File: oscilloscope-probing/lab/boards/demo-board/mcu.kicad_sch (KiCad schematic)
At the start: 3 parts, among them J4 CORTEX_DEBUG_ETM, U4 XC7A35T-2FGG484I, U5 STM32H750XBH6

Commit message: Finished initial demo board schematic
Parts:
- added C59, C60, C61, C67, C68, C69, C71, C72, C73, C74, C75, C76, C77, C78, C79, C80, C81, C82, C83, C84, C85, C86, C87, C88, C89, C99: 0.47 uF, azonenberg_pcb:EIA_0402_CAP_NOSILK, symbol device:C
- added C62, C63, C64, C65, C66, C70: 4.7 uF, azonenberg_pcb:EIA_0603_CAP_NOSILK, symbol device:C
- added D4, D5, D6, D7: GREEN, azonenberg_pcb:EIA_0402_LED, symbol device:LED
- added FB2: MI0603J601R-10, azonenberg_pcb:EIA_0603_INDUCTOR_NOSILK, symbol passive-azonenberg:FERRITE_SMALL2
- added J6: CONN_01X06, symbol conn:CONN_01X06
- added R26: 10K, azonenberg_pcb:EIA_0402_RES_NOSILK, symbol device:R
- added R27: 100K, azonenberg_pcb:EIA_0402_RES_NOSILK, symbol device:R
- added R28, R29, R47, R48, R49, R50: 33, azonenberg_pcb:EIA_0402_RES_NOSILK, symbol device:R
- added R30, R31, R32, R33, R35, R38: 33, symbol device:R
- added R34, R44, R45, R46: 4.7K, symbol device:R
- added R39, R41, R42, R43: 33K, azonenberg_pcb:EIA_0402_RES_NOSILK, symbol device:R
- added SW3, SW4, SW5, SW6, SW7: SWITCH, azonenberg_pcb:SWITCH_RAFI_MICON_5, symbol passive-azonenberg:SWITCH
- added TP12: TESTCLIP, symbol conn:CONN_01X01
- added TP8: CONN_01X03, azonenberg_pcb:CONN_HEADER_2.54MM_1x3_REFLOW, symbol conn:CONN_01X03
- added TP9: U.FL, symbol conn:CONN_COAXIAL
- added U6, U7: ECS-1612MV-250-CN, azonenberg_pcb:OSCILLATOR_1.6x1.2, symbol osc-azonenberg:OSC
- added U8: W25Q80BV, symbol memory-azonenberg:W25Q80BV
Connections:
- net 3V3: now also U5.A6 (VDDLDO), U5.B1 (VBAT), U5.C17 (VDDLDO), U5.E7 (PDR_ON), U5.F17 (VDD33USB), U5.U12 (VDDLDO), C60.1, C61.1, C63.1, C64.1, C65.1, C67.1, C68.1, C69.1, C71.1, C72.1, C73.1, C75.1, C76.1, C77.1, C78.1, C79.1, C80.1, C81.1, C82.1, C83.1, C84.1, C85.1, C86.1, C87.1, C88.1, C89.1, C99.1, FB2.1, R26.1, R44.1, R45.1, R46.1, SW3.1, SW4.1, SW5.1, SW6.1, SW7.1, U6.1 (E/D#), U6.4 (Vdd), U7.1 (E/D#), U7.4 (Vdd), U8.8 (VCC)
- net FPGA_CCLK: now also U8.6 (CLK)
- net GND: now also U5.N1 (VREF_N), C59.1, C60.2, C61.2, C62.2, C63.2, C64.2, C65.2, C66.2, C67.2, C68.2, C69.2, C70.2, C71.2, C72.2, C73.2, C74.2, C75.2, C76.2, C77.2, C78.2, C79.2, C80.2, C81.2, C82.2, C83.2, C84.2, C85.2, C86.2, C87.2, C88.2, C89.2, C99.2, D4.1 (K), D5.1 (K), D6.1 (K), D7.1 (K), J6.1 (P1), R27.1, R34.1, TP8.3 (P3), TP9.2 (Ext), U6.2 (Vss), U7.2 (Vss), U8.4 (GND)
- net JTAG_TCK: now also U5.B14 (PA14)
- net JTAG_TDI: now also U5.A14 (PA15)
- net JTAG_TDO: now also R38.1
- net JTAG_TMS: now also U5.C15 (PA13)
- net MCU_DONE: now also U5.G4 (PF0)
- net MCU_RST_N: now also C59.2, R26.2, R27.2
- net SUPER_I2C_SCL: now also U5.D5 (PB8)
- net SUPER_I2C_SDA: now also U5.D4 (PB9)
- net TRACECLK: now also U5.C3 (PE2)
- net TRACED0: now also U5.D9 (PG13)
- net TRACED1: now also U5.D8 (PG14)
- net TRACED2: now also U5.D12 (PD2)
- net TRACED3: now also U5.C12 (PC12)
- net UART_CTS_N: now also U5.U5 (PB0)
- net UART_RTS_N: now also U5.U15 (PB14)
- net UART_RX: now also U5.N4 (PA1)
- net UART_TX: now also U5.N5 (PA0)
- net MCU_TRIG: now reaches U5.A16 (PI0)
- net MCU_TRIG: now also TP12.1 (P1)
- net DPAD_SEL: now reaches U5.D10 (PJ14)
- net DPAD_SEL: now also SW7.2
- net DPAD_S: now reaches U5.D11 (PJ12)
- net DPAD_S: now also SW6.2
- net DPAD_N: now reaches U5.E10 (PJ13)
- net DPAD_N: now also SW5.2
- net DPAD_E: now reaches U5.K14 (PJ11)
- net DPAD_E: now also SW4.2
- net DPAD_W: now reaches U5.L14 (PJ10)
- net DPAD_W: now also SW3.2
- net MCU_LED0: now reaches U5.N6 (PJ0)
- net MCU_LED0: now also R39.1
- net MCU_LED1: now reaches U5.P6 (PJ1)
- net MCU_LED1: now also R41.1
- net MCU_LED2: now reaches U5.T6 (PJ2)
- net MCU_LED2: now also R42.1
- net MCU_LED3: now reaches U5.U6 (PJ3)
- net MCU_LED3: now also R43.1
- net VCORE: now reaches U5.A7 (VCAP)
- net VCORE: now also U5.D17 (VCAP), U5.U11 (VCAP), C62.1, C66.1, TP9.1 (In)
- net A3V3: now reaches U5.L1 (VDDA)
- net A3V3: now also U5.M1 (VREF_P), C70.1, C74.1, FB2.2
- net CONSOLE_UART_RX: now reaches U5.D14 (PA10)
- net CONSOLE_UART_RX: now also TP8.2 (P2)
- net CONSOLE_UART_TX: now reaches U5.D15 (PA9)
- net CONSOLE_UART_TX: now also TP8.1 (P1)
- net DAC1_OUT2: now reaches U5.T3 (PA5)
- net DAC1_OUT1: now reaches U5.U3 (PA4)
- net MCU_CLK_25MHZ: now reaches U5.J2 (PH0)
- net MCU_CLK_25MHZ: now also R28.1
- net DPY_BS: now reaches U5.H4 (PF3)
- net DPY_DC: now reaches U5.J4 (PF5)
- net DPY_BUSY_N: now reaches U5.J5 (PF4)
- net DPY_SPI_CS_N: now reaches U5.K2 (PF6)
- net DPY_SPI_SCK: now reaches U5.K3 (PF7)
- net DPY_RST_N: now reaches U5.K4 (PF8)
- net DPY_SPI_DATA: now reaches U5.L4 (PF9)
- net FMC_NE3: now reaches U4.AA18 (IO_L17P_T2_A14_D30_14)
- net FMC_NE3: now also U5.G15 (PG6)
- net FPGA_UART_RTS_N: now reaches U4.AA19 (IO_L15P_T2_DQS_RDWR_B_14)
- net FPGA_UART_RTS_N: now also J6.6 (P6)
- net FMC_NOE: now reaches U4.AA20 (IO_L8P_T1_D11_14)
- net FMC_NOE: now also U5.A12 (PD4)
- net FMC_NWE: now reaches U4.AA21 (IO_L8N_T1_D12_14)
- net FMC_NWE: now also U5.A11 (PD5)
- net FMC_AD0: now reaches U4.AB18 (IO_L17N_T2_A13_D29_14)
- net FMC_AD0: now also U5.P16 (PD14)
- net FMC_NE4: now reaches U4.AB20 (IO_L15N_T2_DQS_DOUT_CSO_B_14)
- net FMC_NE4: now also U5.C9 (PG12)
- net FMC_A16: now reaches U4.AB21 (IO_L10P_T1_D14_14)
- net FMC_A16: now also U5.R15 (PD11)
- net FMC_A17: now reaches U4.AB22 (IO_L10N_T1_D15_14)
- net FMC_A17: now also U5.R16 (PD12)
- net FMC_AD11: now reaches U4.N13 (IO_L23P_T3_A03_D19_14)
- net FMC_AD11: now also U5.U10 (PE14)
- net FMC_AD12: now reaches U4.N14 (IO_L23N_T3_A02_D18_14)
- net FMC_AD12: now also U5.R11 (PE15)
- net FMC_AD15: now reaches U4.N15 (IO_25_14)
- net FMC_AD15: now also U5.T16 (PD10)
- net FMC_AD7: now reaches U4.N17 (IO_L21P_T3_DQS_14)
- net FMC_AD7: now also U5.N9 (PE10)
- net FMC_AD3: now reaches U4.P14 (IO_L19P_T3_A10_D26_14)
- net FMC_AD3: now also U5.E12 (PD1)
- net FMC_AD9: now reaches U4.P15 (IO_L22P_T3_A05_D21_14)
- net FMC_AD9: now also U5.R10 (PE12)
- net FMC_AD13: now reaches U4.P16 (IO_L24P_T3_A01_D17_14)
- net FMC_AD13: now also U5.U16 (PD8)
- net FMC_AD8: now reaches U4.P17 (IO_L21N_T3_DQS_A06_D22_14)
- net FMC_AD8: now also U5.P10 (PE11)
- net FPGA_UART_TX: now reaches U4.P19 (IO_L5P_T0_D06_14)
- net FPGA_UART_TX: now also J6.4 (P4)
- net at U4.P21 (IO_L2P_T0_D02_14): now also R32.2
- net at U4.P22 (IO_L1P_T0_D00_MOSI_14): now also R30.2
- net FMC_AD4: now reaches U4.R14 (IO_L19N_T3_A09_D25_VREF_14)
- net FMC_AD4: now also U5.U9 (PE7)
- net FMC_AD10: now reaches U4.R16 (IO_L22N_T3_A04_D20_14)
- net FMC_AD10: now also U5.T10 (PE13)
- net FMC_AD14: now reaches U4.R17 (IO_L24N_T3_A00_D16_14)
- net FMC_AD14: now also U5.T17 (PD9)
- net FMC_AD5: now reaches U4.R18 (IO_L20P_T3_A08_D24_14)
- net FMC_AD5: now also U5.T9 (PE8)
- net FPGA_UART_RX: now reaches U4.R19 (IO_L5N_T0_D07_14)
- net FPGA_UART_RX: now also J6.5 (P5)
- net at U4.R21 (IO_L2N_T0_D03_14): now also R33.2
- net at U4.R22 (IO_L1N_T0_D01_DIN_14): now also R31.2
- net FMC_AD6: now reaches U4.T18 (IO_L20N_T3_A07_D23_14)
- net FMC_AD6: now also U5.P9 (PE9)
- net at U4.T19 (IO_L6P_T0_FCS_B_14): now also R35.2
- net FMC_A21: now reaches U4.T21 (IO_L4P_T0_D04_14)
- net FMC_A21: now also U5.D1 (PE5)
- net FMC_AD1: now reaches U4.U17 (IO_L18P_T2_A12_D28_14)
- net FMC_AD1: now also U5.P15 (PD15)
- net FMC_AD2: now reaches U4.U18 (IO_L18N_T2_A11_D27_14)
- net FMC_AD2: now also U5.D13 (PD0)
- net FMC_A18: now reaches U4.U20 (IO_L11P_T1_SRCC_14)
- net FMC_A18: now also U5.R17 (PD13)
- net FMC_A22: now reaches U4.U21 (IO_L4N_T0_D05_14)
- net FMC_A22: now also U5.E5 (PE6)
- net at U4.U22 (IO_L3P_T0_DQS_PUDC_B_14): now also R34.2
- net FMC_NE1: now reaches U4.V17 (IO_L16P_T2_CSI_B_14)
- net FMC_NE1: now also U5.C11 (PD7)
- net FPGA_UART_CTS_N: now reaches U4.V19 (IO_L14N_T2_SRCC_14)
- net FPGA_UART_CTS_N: now also J6.2 (P2)
- net FMC_A19: now reaches U4.V20 (IO_L11N_T1_SRCC_14)
- net FMC_A19: now also U5.D3 (PE3)
- net FMC_A20: now reaches U4.V22 (IO_L3N_T0_DQS_EMCCLK_14)
- net FMC_A20: now also U5.D2 (PE4)
- net FMC_NE2: now reaches U4.W17 (IO_L16N_T2_A15_D31_14)
- net FMC_NE2: now also U5.E13 (PC8)
- net FPGA_CLK_25MHZ: now reaches U4.W19 (IO_L12P_T1_MRCC_14)
- net FPGA_CLK_25MHZ: now also R29.1
- net FMC_NL_NADV: now reaches U4.W21 (IO_L7P_T1_D09_14)
- net FMC_NL_NADV: now also U5.C5 (PB7)
- net FMC_NWAIT: now reaches U4.W22 (IO_L7N_T1_D10_14)
- net FMC_NWAIT: now also U5.B11 (PD6)
- net FMC_CLK: now reaches U4.Y18 (IO_L13P_T2_MRCC_14)
- net FMC_CLK: now also U5.B12 (PD3)
- net FMC_NBL0: now reaches U4.Y21 (IO_L9P_T1_DQS_14)
- net FMC_NBL0: now also U5.C4 (PE0)
- net FMC_NBL1: now reaches U4.Y22 (IO_L9N_T1_DQS_D13_14)
- net FMC_NBL1: now also U5.B4 (PE1)
- net at U5.C6 (PB3): now also R38.2
- new net: D4.2 (A), R39.2
- new net: R48.2, U8.5 (DI/IO0)
- new net: R29.2, U7.3 (CLK)
- new net: D5.2 (A), R41.2
- new net: R28.2, U6.3 (CLK)
- new net: D6.2 (A), R42.2
- new net: R49.1, U8.2 (DO/IO1)
- new net: R50.1, U8.3 (WP#/IO2)
- new net: R47.2, U8.7 (HOLD#/IO3)
- new net: D7.2 (A), R43.2
- new net QSPI_CS_N: R35.1, R46.2, U8.1 (CS#)
- new net QSPI_DQ0: R30.1, R48.1
- new net QSPI_DQ1: R31.1, R49.2
- new net QSPI_DQ2: R32.1, R44.2, R50.2
- new net QSPI_DQ3: R33.1, R45.2, R47.1
- no-connect marks 8 -> 115
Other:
- added sheet E-paper display (display.kicad_sch)
- note added: "FTDI cable pinout"
- note added: "MCU VDDA decoupling"
- note added: "TRACECLK / A23 unavoidably conflict So limit to 2^22 words (2^23 = 0x80_0000 bytes) of APB address space"
- note added: "VCAP"
- note added: "VDD"
- note added: "VDD33USB"
- note added: "VDDLDO"

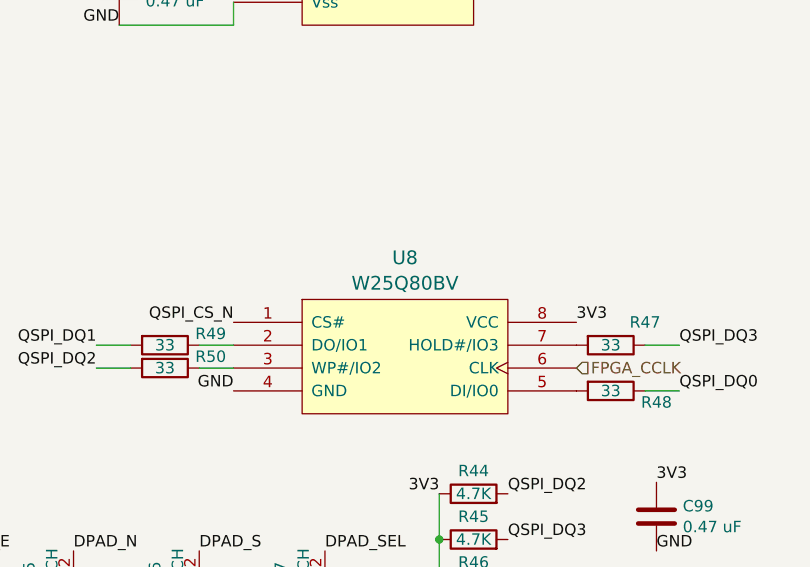
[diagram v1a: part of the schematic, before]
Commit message: Continued initial schematic, assigned footprints
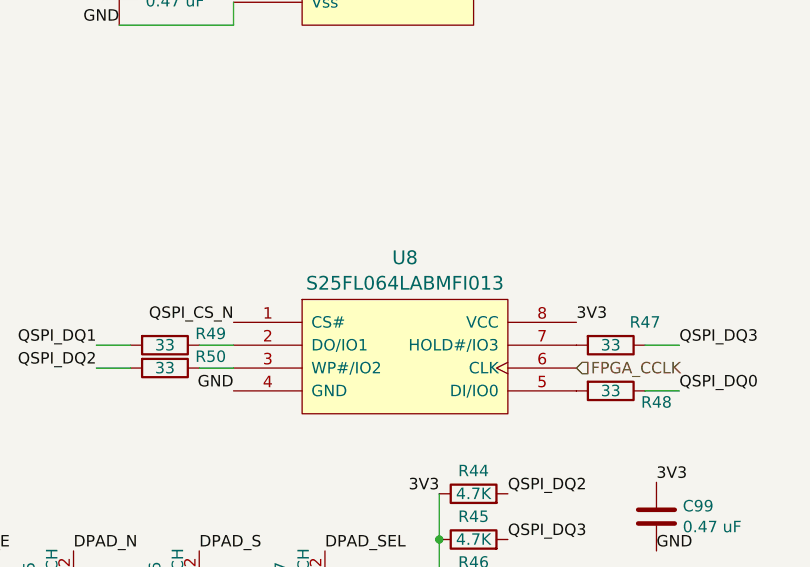
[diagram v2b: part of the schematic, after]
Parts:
- J6: footprint (none) -> azonenberg_pcb:CONN_HEADER_2.54MM_1x6_REFLOW
- R30, R31, R32, R33, R34, R35, R38, R44, R45, R46: footprint (none) -> azonenberg_pcb:EIA_0402_RES_NOSILK
- TP12: footprint (none) -> azonenberg_pcb:TESTPOINT_SMT_KEYSTONE_5016
- TP9: footprint (none) -> azonenberg_pcb:CONN_U.FL_TE_1909763-1
- U4: footprint (none) -> azonenberg_pcb:BGA_484_22x22_FULLARRAY_1MM
- U5: footprint (none) -> azonenberg_pcb:BGA_265_14x14_DEPOP_0.8MM
- U8: value W25Q80BV -> S25FL064LABMFI013; footprint (none) -> azonenberg_pcb:SOIC_8_5.3MM
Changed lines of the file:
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@@
 			)
 		)
-		(property "Footprint" ""
+		(property "Footprint" "azonenberg_pcb:BGA_265_14x14_DEPOP_0.8MM"
 			(at 111.76 209.55 0)
 			(effects
@@
 			)
 		)
-		(property "Footprint" ""
+		(property "Footprint" "azonenberg_pcb:BGA_265_14x14_DEPOP_0.8MM"
 			(at 111.76 256.54 0)
 			(effects
@@
 			)
 		)
-		(property "Footprint" ""
+		(property "Footprint" "azonenberg_pcb:EIA_0402_RES_NOSILK"
 			(at 31.75 80.518 90)
 			(effects
@@
 			)
 		)
-		(property "Footprint" ""
+		(property "Footprint" "azonenberg_pcb:BGA_265_14x14_DEPOP_0.8MM"
 			(at 254 78.74 0)
 			(effects
@@
 			)
 		)
-		(property "Footprint" ""
+		(property "Footprint" "azonenberg_pcb:EIA_0402_RES_NOSILK"
 			(at 185.42 274.828 90)
 			(effects
@@
 			)
 		)
-		(property "Footprint" ""
+		(property "Footprint" "azonenberg_pcb:EIA_0402_RES_NOSILK"
 			(at 341.63 33.528 90)
 			(effects
@@
 			)
 		)
-		(property "Footprint" ""
+		(property "Footprint" "azonenberg_pcb:BGA_265_14x14_DEPOP_0.8MM"
 			(at 162.56 43.18 0)
 			(effects
@@
 			)
 		)
-		(property "Footprint" ""
+		(property "Footprint" "azonenberg_pcb:BGA_265_14x14_DEPOP_0.8MM"
 			(at 39.37 63.5 0)
 			(effects
@@
 			)
 		)
-		(property "Footprint" ""
+		(property "Footprint" "azonenberg_pcb:EIA_0402_RES_NOSILK"
 			(at 185.42 264.668 90)
 			(effects
@@
 			)
 		)
-		(property "Footprint" ""
+		(property "Footprint" "azonenberg_pcb:BGA_265_14x14_DEPOP_0.8MM"
 			(at 254 209.55 0)
 			(effects
@@
 			)
 		)
-		(property "Footprint" ""
+		(property "Footprint" "azonenberg_pcb:BGA_265_14x14_DEPOP_0.8MM"
 			(at 111.76 157.48 0)
 			(effects
@@
 			)
 		)
-		(property "Footprint" ""
+		(property "Footprint" "azonenberg_pcb:EIA_0402_RES_NOSILK"
 			(at 341.63 56.388 90)
 			(effects
@@
 			)
 		)
-		(property "Footprint" ""
+		(property "Footprint" "azonenberg_pcb:CONN_U.FL_TE_1909763-1"
 			(at 325.12 160.02 0)
 			(effects
@@
 			)
 		)
-		(property "Footprint" ""
+		(property "Footprint" "azonenberg_pcb:BGA_265_14x14_DEPOP_0.8MM"
 			(at 111.76 63.5 0)
 			(effects
@@
 			)
 		)
-		(property "Footprint" ""
+		(property "Footprint" "azonenberg_pcb:BGA_484_22x22_FULLARRAY_1MM"
 			(at 353.06 158.75 0)
 			(effects
@@
 					(size 1.524 1.524)
 				)
+				(hide yes)
 			)
 		)
@@
 			)
 		)
-		(property "Footprint" ""
+		(property "Footprint" "azonenberg_pcb:EIA_0402_RES_NOSILK"
 			(at 341.63 36.068 90)
 			(effects
@@
 			)
 		)
-		(property "Value" "W25Q80BV"
+		(property "Value" "S25FL064LABMFI013"
 			(at 177.8 239.5025 0)
 			(effects
@@
 			)
 		)
-		(property "Footprint" ""
+		(property "Footprint" "azonenberg_pcb:SOIC_8_5.3MM"
 			(at 177.8 254 0)
 			(effects
@@
 					(size 1.524 1.524)
 				)
+				(hide yes)
 			)
 		)
@@
 			)
 		)
-		(property "Footprint" ""
+		(property "Footprint" "azonenberg_pcb:BGA_265_14x14_DEPOP_0.8MM"
 			(at 254 172.72 0)
 			(effects
@@
 			)
 		)
-		(property "Footprint" ""
+		(property "Footprint" "azonenberg_pcb:BGA_265_14x14_DEPOP_0.8MM"
 			(at 39.37 209.55 0)
 			(effects
@@
 			)
 		)
-		(property "Footprint" ""
+		(property "Footprint" "azonenberg_pcb:BGA_265_14x14_DEPOP_0.8MM"
 			(at 254 148.59 0)
 			(effects
@@
 			)
 		)
-		(property "Footprint" ""
+		(property "Footprint" "azonenberg_pcb:EIA_0402_RES_NOSILK"
 			(at 341.63 38.608 90)
 			(effects
@@
 			)
 		)
-		(property "Footprint" ""
+		(property "Footprint" "azonenberg_pcb:BGA_265_14x14_DEPOP_0.8MM"
 			(at 39.37 162.56 0)
 			(effects
@@
 			)
 		)
-		(property "Footprint" ""
+		(property "Footprint" "azonenberg_pcb:BGA_265_14x14_DEPOP_0.8MM"
 			(at 111.76 110.49 0)
 			(effects
@@
 			)
 		)
-		(property "Footprint" ""
+		(property "Footprint" "azonenberg_pcb:BGA_265_14x14_DEPOP_0.8MM"
 			(at 39.37 110.49 0)
 			(effects
@@
 			)
 		)
-		(property "Footprint" ""
+		(property "Footprint" "azonenberg_pcb:EIA_0402_RES_NOSILK"
 			(at 185.42 269.748 90)
 			(effects
@@
 			)
 		)
-		(property "Footprint" ""
+		(property "Footprint" "azonenberg_pcb:CONN_HEADER_2.54MM_1x6_REFLOW"
 			(at 374.65 171.45 0)
 			(effects
@@
 			)
 		)
-		(property "Footprint" ""
+		(property "Footprint" "azonenberg_pcb:EIA_0402_RES_NOSILK"
 			(at 341.63 41.148 90)
 			(effects
@@
 			)
 		)
-		(property "Footprint" ""
+		(property "Footprint" "azonenberg_pcb:EIA_0402_RES_NOSILK"
 			(at 341.63 30.988 90)
 			(effects
@@
 			)
 		)
-		(property "Footprint" ""
+		(property "Footprint" "azonenberg_pcb:TESTPOINT_SMT_KEYSTONE_5016"
 			(at 83.82 170.18 0)
 			(effects
@@
 			)
 		)
-		(property "Footprint" ""
+		(property "Footprint" "azonenberg_pcb:BGA_265_14x14_DEPOP_0.8MM"
 			(at 39.37 256.54 0)
 			(effects

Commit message: Continued demo board layout
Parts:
- added C123: 0.47 uF, azonenberg_pcb:EIA_0402_CAP_NOSILK, symbol device:C
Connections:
- net A3V3: now also C123.1
- net GND: now also C123.2
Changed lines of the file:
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@@
 	)
 	(junction
+		(at 318.77 237.49)
+		(diameter 0)
+		(color 0 0 0 0)
+	)
+	(junction
 		(at 158.75 185.42)
 		(diameter 0)
@@
 	)
 	(junction
+		(at 318.77 245.11)
+		(diameter 0)
+		(color 0 0 0 0)
+	)
+	(junction
 		(at 303.53 167.64)
 		(diameter 0)
@@
 	(wire
 		(pts
+			(xy 318.77 245.11) (xy 334.01 245.11)
+		)
+		(stroke
+			(width 0)
+			(type default)
+		)
+	)
+	(wire
+		(pts
 			(xy 250.19 106.68) (xy 250.19 109.22)
 		)
@@
 	(wire
 		(pts
+			(xy 318.77 237.49) (xy 334.01 237.49)
+		)
+		(stroke
+			(width 0)
+			(type default)
+		)
+	)
+	(wire
+		(pts
 			(xy 270.51 91.44) (xy 270.51 93.98)
 		)
@@
 				)
 			)
+		)
+	)
+	(symbol
+		(lib_id "device:C")
+		(at 334.01 241.3 0)
+		(unit 1)
+		(exclude_from_sim no)
+		(in_bom yes)
+		(on_board yes)
+		(dnp no)
+		(fields_autoplaced yes)
+		(property "Reference" "C123"
+			(at 336.931 240.3915 0)
+			(effects
+				(font
+					(size 1.27 1.27)
+				)
+				(justify left)
+			)
+		)
+		(property "Value" "0.47 uF"
+			(at 336.931 243.1666 0)
+			(effects
+				(font
+					(size 1.27 1.27)
+				)
+				(justify left)
+			)
+		)
+		(property "Footprint" "azonenberg_pcb:EIA_0402_CAP_NOSILK"
+			(at 334.9752 245.11 0)
+			(effects
+				(font
+					(size 1.27 1.27)
+				)
+				(hide yes)
+			)
+		)
+		(property "Datasheet" ""
+			(at 334.01 241.3 0)
+			(effects
+				(font
+					(size 1.27 1.27)
+				)
+				(hide yes)
+			)
+		)
+		(property "Description" ""
+			(at 334.01 241.3 0)
+			(effects
+				(font
+					(size 1.27 1.27)
+				)
+				(hide yes)
+			)
+		)
+		(pin "1"
+		)
+		(pin "2"
+		)
+		(instances
+			(project "demo-board"
+				(path "/aa2d82c6-7ba7-4266-9b47-ed3339e6c556/a3b16bfb-b7c6-40a4-acca-70d1a835c16b"
+					(reference "C123")
+					(unit 1)
+				)
+			)

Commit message: Continued demo board layout
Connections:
- net FMC_A16: now also U4.AA20 (IO_L8P_T1_D11_14); no longer U4.AB21 (IO_L10P_T1_D14_14)
- net FMC_A17: now also U4.AA18 (IO_L17P_T2_A14_D30_14); no longer U4.AB22 (IO_L10N_T1_D15_14)
- net FMC_A18: now also U4.AB18 (IO_L17N_T2_A13_D29_14); no longer U4.U20 (IO_L11P_T1_SRCC_14)
- net FMC_A20: now also U4.R18 (IO_L20P_T3_A08_D24_14); no longer U4.V22 (IO_L3N_T0_DQS_EMCCLK_14)
- net FMC_A22: now also U4.P15 (IO_L22P_T3_A05_D21_14); no longer U4.U21 (IO_L4N_T0_D05_14)
- net FMC_AD0: now also U4.W17 (IO_L16N_T2_A15_D31_14); no longer U4.AB18 (IO_L17N_T2_A13_D29_14)
- net FMC_AD1: now also U4.AA21 (IO_L8N_T1_D12_14); no longer U4.U17 (IO_L18P_T2_A12_D28_14)
- net FMC_AD10: now also U4.W22 (IO_L7N_T1_D10_14); no longer U4.R16 (IO_L22N_T3_A04_D20_14)
- net FMC_AD11: now also U4.Y21 (IO_L9P_T1_DQS_14); no longer U4.N13 (IO_L23P_T3_A03_D19_14)
- net FMC_AD12: now also U4.Y22 (IO_L9N_T1_DQS_D13_14); no longer U4.N14 (IO_L23N_T3_A02_D18_14)
- net FMC_AD13: now also U4.AB21 (IO_L10P_T1_D14_14); no longer U4.P16 (IO_L24P_T3_A01_D17_14)
- net FMC_AD14: now also U4.AB20 (IO_L15N_T2_DQS_DOUT_CSO_B_14); no longer U4.R17 (IO_L24N_T3_A00_D16_14)
- net FMC_AD15: now also U4.AB22 (IO_L10N_T1_D15_14); no longer U4.N15 (IO_25_14)
- net FMC_AD4: now also U4.W21 (IO_L7P_T1_D09_14); no longer U4.R14 (IO_L19N_T3_A09_D25_VREF_14)
- net FMC_AD5: now also U4.V22 (IO_L3N_T0_DQS_EMCCLK_14); no longer U4.R18 (IO_L20P_T3_A08_D24_14)
- net FMC_AD6: now also U4.P17 (IO_L21N_T3_DQS_A06_D22_14); no longer U4.T18 (IO_L20N_T3_A07_D23_14)
- net FMC_AD8: now also U4.T18 (IO_L20N_T3_A07_D23_14); no longer U4.P17 (IO_L21N_T3_DQS_A06_D22_14)
- net FMC_AD9: now also U4.U21 (IO_L4N_T0_D05_14); no longer U4.P15 (IO_L22P_T3_A05_D21_14)
- net FMC_NBL0: now also U4.N13 (IO_L23P_T3_A03_D19_14); no longer U4.Y21 (IO_L9P_T1_DQS_14)
- net FMC_NBL1: now also U4.N14 (IO_L23N_T3_A02_D18_14); no longer U4.Y22 (IO_L9N_T1_DQS_D13_14)
- net FMC_NE2: now also U4.U20 (IO_L11P_T1_SRCC_14); no longer U4.W17 (IO_L16N_T2_A15_D31_14)
- net FMC_NE3: now also U4.N15 (IO_25_14); no longer U4.AA18 (IO_L17P_T2_A14_D30_14)
- net FMC_NE4: now also U4.R17 (IO_L24N_T3_A00_D16_14); no longer U4.AB20 (IO_L15N_T2_DQS_DOUT_CSO_B_14)
- net FMC_NL_NADV: now also U4.R14 (IO_L19N_T3_A09_D25_VREF_14); no longer U4.W21 (IO_L7P_T1_D09_14)
- net FMC_NOE: now also U4.P16 (IO_L24P_T3_A01_D17_14); no longer U4.AA20 (IO_L8P_T1_D11_14)
- net FMC_NWAIT: now also U4.R16 (IO_L22N_T3_A04_D20_14); no longer U4.W22 (IO_L7N_T1_D10_14)
- net FMC_NWE: now also U4.U17 (IO_L18P_T2_A12_D28_14); no longer U4.AA21 (IO_L8N_T1_D12_14)
- net MCU_LED0: now also U5.A2 (PI6); no longer U5.N6 (PJ0)
- net MCU_LED1: now also U5.A3 (PI5); no longer U5.P6 (PJ1)
- net MCU_LED2: now also U5.A4 (PI4); no longer U5.T6 (PJ2)
- net MCU_LED3: now also U5.A5 (PB5); no longer U5.U6 (PJ3)
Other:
- company: (none) -> Antikernel Labs
- title: (none) -> Oscilloscope Demo Board
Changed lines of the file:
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@@
 	(generator_version "9.0")
 	(paper "A3")
+	(title_block
+		(title "Oscilloscope Demo Board")
+		(date "2026-08-08")
+		(rev "0.1")
+		(company "Antikernel Labs")
+		(comment 1 "Andrew D. Zonenberg")
+	)
 	(text "TRACECLK / A23\nunavoidably conflict\nSo limit to 2^22 words\n(2^23 = 0x80_0000 bytes)\nof APB address space"
 		(exclude_from_sim no)
@@
 	)
 	(no_connect
-		(at 107.95 182.88)
-	)
-	(no_connect
 		(at 35.56 156.21)
 	)
@@
 	)
 	(no_connect
+		(at 107.95 217.17)
+	)
+	(no_connect
 		(at 107.95 151.13)
 	)
@@
 	)
 	(no_connect
+		(at 107.95 222.25)
+	)
+	(no_connect
 		(at 158.75 24.13)
 	)
@@
 	)
 	(no_connect
-		(at 35.56 83.82)
-	)
-	(no_connect
 		(at 107.95 133.35)
 	)
 	(no_connect
-		(at 107.95 185.42)
-	)
-	(no_connect
 		(at 35.56 81.28)
 	)
@@
 	)
 	(no_connect
+		(at 107.95 224.79)
+	)
+	(no_connect
 		(at 35.56 44.45)
 	)
@@
 	)
 	(no_connect
-		(at 107.95 180.34)
-	)
-	(no_connect
 		(at 107.95 234.95)
 	)
@@
 	)
 	(no_connect
+		(at 107.95 219.71)
+	)
+	(no_connect
 		(at 107.95 62.23)
 	)
@@
 	)
 	(label "FMC_A17"
-		(at 347.98 77.47 180)
+		(at 347.98 110.49 180)
 		(effects
 			(font
@@
 	)
 	(label "FMC_A22"
-		(at 347.98 46.99 180)
+		(at 347.98 135.89 180)
 		(effects
 			(font
@@
 	)
 	(label "MCU_LED3"
-		(at 107.95 224.79 180)
+		(at 35.56 83.82 180)
 		(effects
 			(font
@@
 	)
 	(label "FMC_AD14"
-		(at 347.98 148.59 180)
+		(at 347.98 102.87 180)
 		(effects
 			(font
@@
 	)
 	(label "MCU_LED2"
-		(at 107.95 222.25 180)
+		(at 107.95 180.34 180)
 		(effects
 			(font
@@
 	)
 	(label "FMC_A16"
-		(at 347.98 74.93 180)
+		(at 347.98 64.77 180)
 		(effects
 			(font
@@
 	)
 	(label "FMC_NWE"
-		(at 347.98 67.31 180)
+		(at 347.98 115.57 180)
 		(effects
 			(font
@@
 	)
 	(label "FMC_AD1"
-		(at 347.98 115.57 180)
+		(at 347.98 67.31 180)
 		(effects
 			(font
@@
 	)
 	(label "FMC_A20"
-		(at 347.98 41.91 180)
+		(at 347.98 125.73 180)
 		(effects
 			(font
@@
 	)
 	(label "FMC_NE4"
-		(at 347.98 102.87 180)
+		(at 347.98 148.59 180)
 		(effects
 			(font
@@
 	)
 	(label "FMC_NWAIT"
-		(at 347.98 62.23 180)
+		(at 347.98 138.43 180)
 		(effects
 			(font
@@
 	)
 	(label "FMC_NL_NADV"
-		(at 347.98 59.69 180)
+		(at 347.98 123.19 180)
 		(effects
 			(font
@@
 	)
 	(label "FMC_NBL0"
-		(at 347.98 69.85 180)
+		(at 347.98 140.97 180)
 		(effects
 			(font
@@
 	)
 	(label "FMC_AD9"
-		(at 347.98 135.89 180)
+		(at 347.98 46.99 180)
 		(effects
 			(font
@@
 	)
 	(label "FMC_A18"
-		(at 347.98 80.01 180)
+		(at 347.98 113.03 180)
 		(effects
 			(font
@@
 	)
 	(label "FMC_AD15"
-		(at 347.98 151.13 180)
+		(at 347.98 77.47 180)
 		(effects
 			(font
@@
 	)
 	(label "FMC_NBL1"
-		(at 347.98 72.39 180)
+		(at 347.98 143.51 180)
 		(effects
 			(font
@@
 	)
 	(label "FMC_AD4"
-		(at 347.98 123.19 180)
+		(at 347.98 59.69 180)
 		(effects
 			(font
@@
 	)
 	(label "FMC_NE2"
-		(at 347.98 107.95 180)
+		(at 347.98 80.01 180)
 		(effects
 			(font
@@
 	)
 	(label "FMC_AD6"
-		(at 347.98 128.27 180)
+		(at 347.98 133.35 180)
 		(effects
 			(font
@@
 	)
 	(label "FMC_AD12"
-		(at 347.98 143.51 180)
+		(at 347.98 72.39 180)
 		(effects
 			(font
@@
 	)
 	(label "FMC_NE3"
-		(at 347.98 110.49 180)
+		(at 347.98 151.13 180)
 		(effects
 			(font
@@
 	)
 	(label "FMC_NOE"
-		(at 347.98 64.77 180)
+		(at 347.98 146.05 180)
 		(effects
 			(font
@@
 	)
 	(label "MCU_LED0"
-		(at 107.95 217.17 180)
+		(at 107.95 185.42 180)
 		(effects
 			(font
@@
 	)
 	(label "FMC_AD13"
-		(at 347.98 146.05 180)
+		(at 347.98 74.93 180)
 		(effects
 			(font
@@
 	)
 	(label "FMC_AD10"
-		(at 347.98 138.43 180)
+		(at 347.98 62.23 180)
 		(effects
 			(font
@@
 	)
 	(label "MCU_LED1"
-		(at 107.95 219.71 180)
+		(at 107.95 182.88 180)
 		(effects
 			(font
@@
 	)
 	(label "FMC_AD0"
-		(at 347.98 113.03 180)
+		(at 347.98 107.95 180)
 		(effects
 			(font
@@
 	)
 	(label "FMC_AD5"
-		(at 347.98 125.73 180)
+		(at 347.98 41.91 180)
 		(effects
 			(font
@@
 	)
 	(label "FMC_AD8"
-		(at 347.98 133.35 180)
+		(at 347.98 128.27 180)
 		(effects
 			(font
@@
 	)
 	(label "FMC_AD11"
-		(at 347.98 140.97 180)
+		(at 347.98 69.85 180)
 		(effects
 			(font
